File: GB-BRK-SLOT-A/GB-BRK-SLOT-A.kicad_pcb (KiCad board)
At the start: 2 copper layers, 81 x 80 mm, 24 parts, among them J1 Conn_02x16_Odd_Even, J2 Conn_02x16_Odd_Even, J3 GameBoy_Cartridge, J4 Conn_02x02_Odd_Even

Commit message: Update GB-BRK-SLOT-A
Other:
- outline, holes or cut-outs redrawn
- board text added: "GB-BRK-SLOT-A v1.1 https://gekkio.fi"
- board text removed: "GB-BRK-SLOT-A v1.0 https://gekkio.fi"
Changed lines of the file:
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@@
-(kicad_pcb (version 20171130) (host pcbnew 5.0.2-bee76a0~70~ubuntu18.10.1)
+(kicad_pcb (version 20171130) (host pcbnew 5.1.5-52549c5~84~ubuntu19.10.1)
   (general
     (thickness 1.2)
-    (drawings 50)
+    (drawings 54)
     (tracks 478)
     (zones 0)
@@
   (title_block
     (title GB-BRK-SLOT-A)
-    (rev v1.0)
+    (rev v1.1)
     (company https://gekkio.fi)
   )
@@
     (zone_45_only yes)
     (trace_min 0.2)
-    (segment_width 0.2)
-    (edge_width 0.15)
     (via_size 0.6)
     (via_drill 0.4)
@@
     (uvia_min_size 0.2)
     (uvia_min_drill 0.1)
+    (edge_width 0.15)
+    (segment_width 0.2)
     (pcb_text_width 0.3)
     (pcb_text_size 1.5 1.5)
@@
       (net 3 GND))
   )
+  (gr_arc (start 126 148) (end 126 150) (angle -90) (layer Edge.Cuts) (width 0.15))
+  (gr_arc (start 49 148) (end 47 148) (angle -90) (layer Edge.Cuts) (width 0.15))
+  (gr_arc (start 49 72) (end 49 70) (angle -90) (layer Edge.Cuts) (width 0.15))
+  (gr_arc (start 126 72) (end 128 72) (angle -90) (layer Edge.Cuts) (width 0.15))
   (gr_text VCC (at 55.5 102.1 90) (layer F.SilkS)
     (effects (font (size 1.5 1.5) (thickness 0.3)))
@@
     (effects (font (size 1.5 1.5) (thickness 0.3)) (justify right))
   )
-  (gr_text "GB-BRK-SLOT-A v1.0\nhttps://gekkio.fi" (at 87.5 131.4) (layer F.SilkS)
+  (gr_text "GB-BRK-SLOT-A v1.1\nhttps://gekkio.fi" (at 87.5 131.4) (layer F.SilkS)
     (effects (font (size 1.5 1.5) (thickness 0.3)))
   )
@@
     (effects (font (size 1.5 1.5) (thickness 0.3)) (justify right))
   )
-  (gr_line (start 128 70) (end 128 150) (layer Edge.Cuts) (width 0.15))
-  (gr_line (start 47 70) (end 128 70) (layer Edge.Cuts) (width 0.15))
-  (gr_line (start 47 150) (end 128 150) (layer Edge.Cuts) (width 0.15))
-  (gr_line (start 47 70) (end 47 150) (layer Edge.Cuts) (width 0.15))
+  (gr_line (start 128 72) (end 128 148) (layer Edge.Cuts) (width 0.15))
+  (gr_line (start 49 70) (end 126 70) (layer Edge.Cuts) (width 0.15))
+  (gr_line (start 49 150) (end 126 150) (layer Edge.Cuts) (width 0.15))
+  (gr_line (start 47 72) (end 47 148) (layer Edge.Cuts) (width 0.15))
   (segment (start 65.7875 146.8) (end 65.7875 148.4) (width 0.32) (layer F.Cu) (net 1) (status 30))
   (segment (start 67.247919 117.46) (end 68.45 117.46) (width 0.8) (layer F.Cu) (net 2) (status 20))

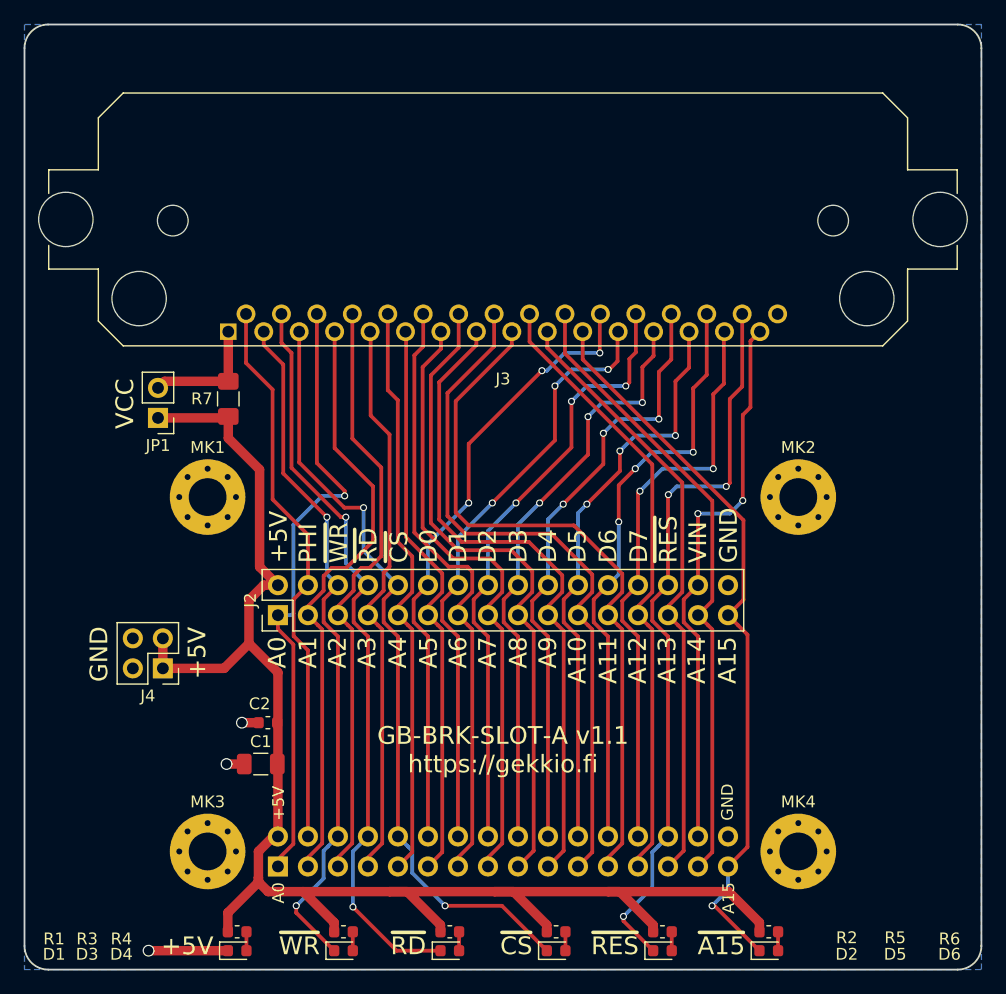
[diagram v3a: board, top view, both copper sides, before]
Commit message: Upgrade most projects to KiCad 6
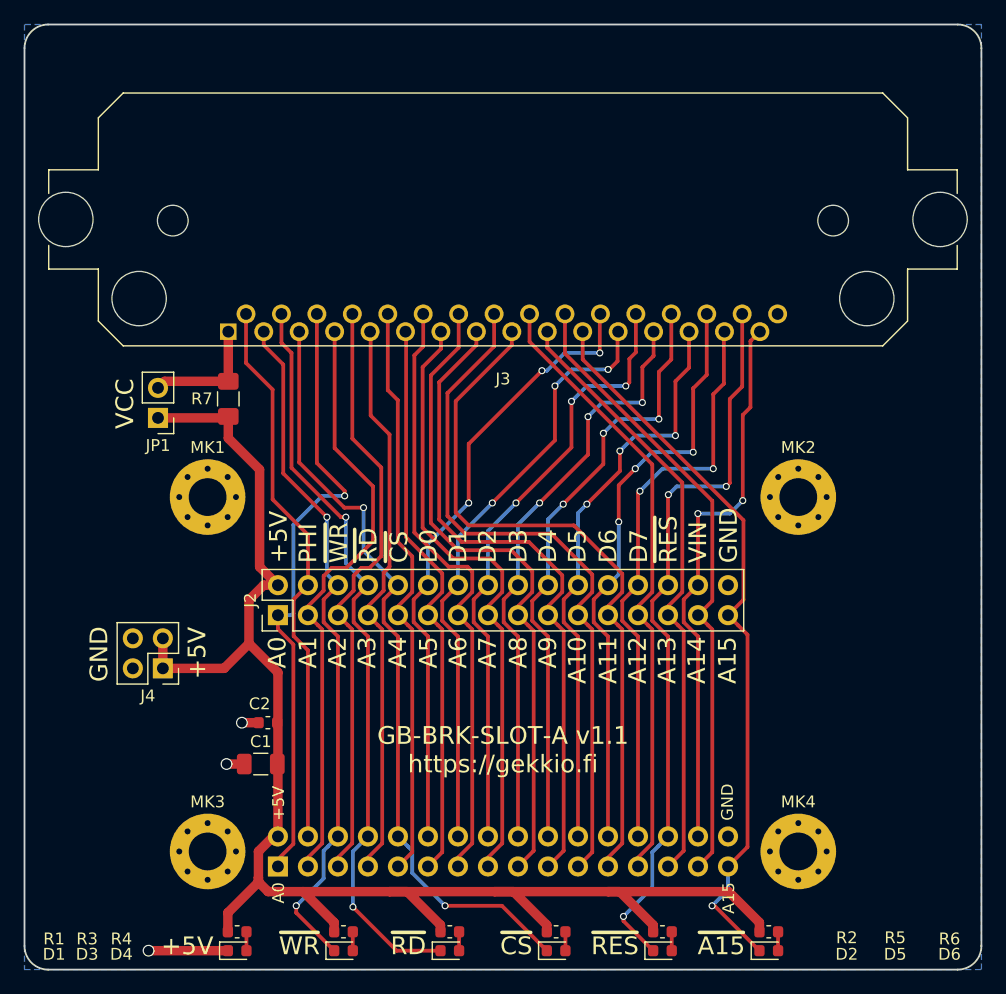
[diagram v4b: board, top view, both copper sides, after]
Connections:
- net /~CS renamed /~{CS}
- net /~RD renamed /~{RD}
- net /~RES renamed /~{RES}
- net /~WR renamed /~{WR}
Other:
- net class Default removed
- net class Power removed
- board text added: "~{A15}"
- board text added: "~{CS}"
- board text added: "~{RD}"
- board text added: "~{RES}"
- board text added: "~{WR}"
- board text removed: "~A15"
- board text removed: "~CS"
- board text removed: "~RD"
- board text removed: "~RES"
- board text removed: "~WR"
